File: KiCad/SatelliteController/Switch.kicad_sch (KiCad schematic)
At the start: 22 parts, among them SW1 SW_Push, SW11 SW_Push, SW17 SW_Push, SW18 SW_Push, SW19 SW_Push, SW2 SW_Push, SW20 SW_Push, SW21 SW_Push, SW22 SW_Push, SW23 SW_Push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

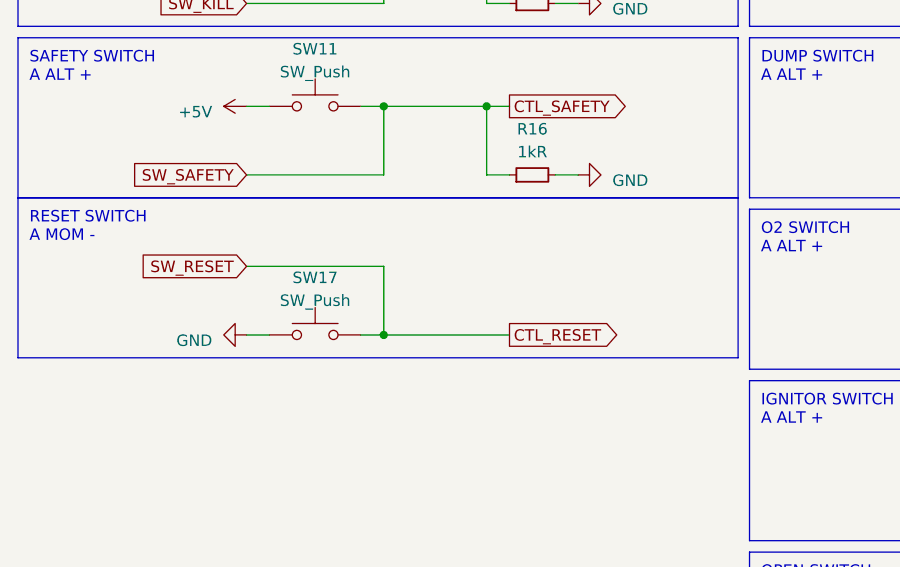
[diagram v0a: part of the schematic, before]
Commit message: サテコンのボード図を作成
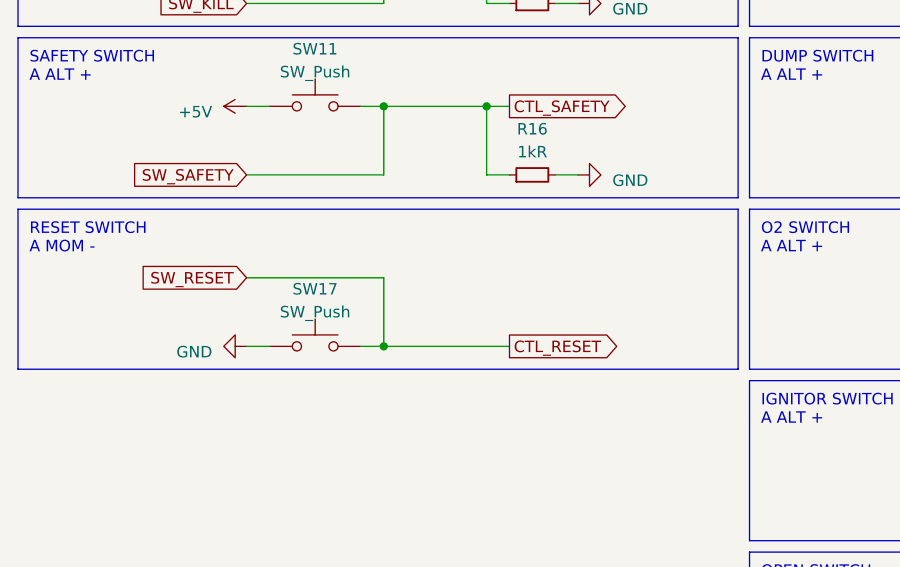
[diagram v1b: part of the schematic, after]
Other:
- moved on the sheet: SW17
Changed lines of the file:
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@@
   (junction (at 53.34 58.42) (diameter 0) (color 0 0 0 0)
   )
-  (junction (at 53.34 83.82) (diameter 0) (color 0 0 0 0)
+  (junction (at 53.34 85.09) (diameter 0) (color 0 0 0 0)
   )
   (junction (at 64.77 39.37) (diameter 0) (color 0 0 0 0)
@@
     (stroke (width 0) (type default))
   )
-  (wire (pts (xy 40.64 83.82) (xy 38.1 83.82))
+  (wire (pts (xy 40.64 85.09) (xy 38.1 85.09))
     (stroke (width 0) (type default))
   )
@@
     (stroke (width 0) (type default))
   )
-  (wire (pts (xy 53.34 76.2) (xy 53.34 83.82))
+  (wire (pts (xy 53.34 77.47) (xy 53.34 85.09))
     (stroke (width 0) (type default))
   )
@@
     (stroke (width 0) (type default))
   )
-  (wire (pts (xy 53.34 83.82) (xy 67.31 83.82))
+  (wire (pts (xy 53.34 85.09) (xy 67.31 85.09))
     (stroke (width 0) (type default))
   )
@@
     (stroke (width 0) (type default))
   )
-  (wire (pts (xy 50.8 83.82) (xy 53.34 83.82))
+  (wire (pts (xy 50.8 85.09) (xy 53.34 85.09))
     (stroke (width 0) (type default))
   )
@@
     (stroke (width 0) (type default))
   )
-  (wire (pts (xy 38.1 76.2) (xy 53.34 76.2))
+  (wire (pts (xy 38.1 77.47) (xy 53.34 77.47))
     (stroke (width 0) (type default))
   )
@@
     (fill (type none))
   )
-  (rectangle (start 12.7 68.58) (end 92.71 86.36)
+  (rectangle (start 12.7 69.85) (end 92.71 87.63)
     (stroke (width 0) (type default))
     (fill (type none))
@@
     (effects (font (size 1.27 1.27)) (justify left bottom))
   )
-  (text "RESET SWITCH\nA MOM -" (at 13.97 73.66 0)
+  (text "RESET SWITCH\nA MOM -" (at 13.97 74.93 0)
     (effects (font (size 1.27 1.27)) (justify left bottom))
   )
@@
     )
   )
-  (global_label "CTL_RESET" (shape output) (at 67.31 83.82 0) (fields_autoplaced)
-    (effects (font (size 1.27 1.27)) (justify left))
-    (property "Intersheetrefs" "${INTERSHEET_REFS}" (at 80.1942 83.82 0)
+  (global_label "CTL_RESET" (shape output) (at 67.31 85.09 0) (fields_autoplaced)
+    (effects (font (size 1.27 1.27)) (justify left))
+    (property "Intersheetrefs" "${INTERSHEET_REFS}" (at 80.1942 85.09 0)
       (effects (font (size 1.27 1.27)) (justify left) hide)
     )
@@
     )
   )
-  (global_label "SW_RESET" (shape input) (at 38.1 76.2 180) (fields_autoplaced)
+  (global_label "SW_RESET" (shape input) (at 38.1 77.47 180) (fields_autoplaced)
     (effects (font (size 1.27 1.27)) (justify right))
-    (property "Intersheetrefs" "${INTERSHEET_REFS}" (at 25.8206 76.2 0)
+    (property "Intersheetrefs" "${INTERSHEET_REFS}" (at 25.8206 77.47 0)
       (effects (font (size 1.27 1.27)) (justify right) hide)
     )
@@
     )
   )
-  (symbol (lib_id "power:GND") (at 38.1 83.82 270) (unit 1)
-    (in_bom yes) (on_board yes) (dnp no) (fields_autoplaced)
-    (property "Reference" "#PWR0104" (at 31.75 83.82 0)
-      (effects (font (size 1.27 1.27)) hide)
-    )
-    (property "Value" "GND" (at 34.29 84.455 90)
+  (symbol (lib_id "power:GND") (at 38.1 85.09 270) (unit 1)
+    (in_bom yes) (on_board yes) (dnp no) (fields_autoplaced)
+    (property "Reference" "#PWR0104" (at 31.75 85.09 0)
+      (effects (font (size 1.27 1.27)) hide)
+    )
+    (property "Value" "GND" (at 34.29 85.725 90)
       (effects (font (size 1.27 1.27)) (justify right))
     )
-    (property "Footprint" "" (at 38.1 83.82 0)
-      (effects (font (size 1.27 1.27)) hide)
-    )
-    (property "Datasheet" "" (at 38.1 83.82 0)
+    (property "Footprint" "" (at 38.1 85.09 0)
+      (effects (font (size 1.27 1.27)) hide)
+    )
+    (property "Datasheet" "" (at 38.1 85.09 0)
       (effects (font (size 1.27 1.27)) hide)
     )
@@
     )
   )
-  (symbol (lib_id "Switch:SW_Push") (at 45.72 83.82 0) (unit 1)
-    (in_bom yes) (on_board yes) (dnp no) (fields_autoplaced)
-    (property "Reference" "SW17" (at 45.72 77.47 0)
-      (effects (font (size 1.27 1.27)))
-    )
-    (property "Value" "SW_Push" (at 45.72 80.01 0)
-      (effects (font (size 1.27 1.27)))
-    )
-    (property "Footprint" "TSRP_Button_Switch_SMD:TVAF06-A020B-R" (at 45.72 78.74 0)
-      (effects (font (size 1.27 1.27)) hide)
-    )
-    (property "Datasheet" "https://akizukidenshi.com/catalog/g/gP-14888/" (at 45.72 78.74 0)
-      (effects (font (size 1.27 1.27)) hide)
-    )
+  (symbol (lib_id "Switch:SW_Push") (at 45.72 85.09 0) (unit 1)
+    (in_bom yes) (on_board yes) (dnp no) (fields_autoplaced)
+    (property "Reference" "SW17" (at 45.72 78.74 0)
+      (effects (font (size 1.27 1.27)))
+    )
+    (property "Value" "SW_Push" (at 45.72 81.28 0)
+      (effects (font (size 1.27 1.27)))
+    )
+    (property "Footprint" "TSRP_Button_Switch_SMD:TVAF06-A020B-R" (at 45.72 80.01 0)
+      (effects (font (size 1.27 1.27)) hide)
+    )
+    (property "Datasheet" "https://akizukidenshi.com/catalog/g/gP-14888/" (at 45.72 80.01 0)
+      (effects (font (size 1.27 1.27)) hide)
+    )

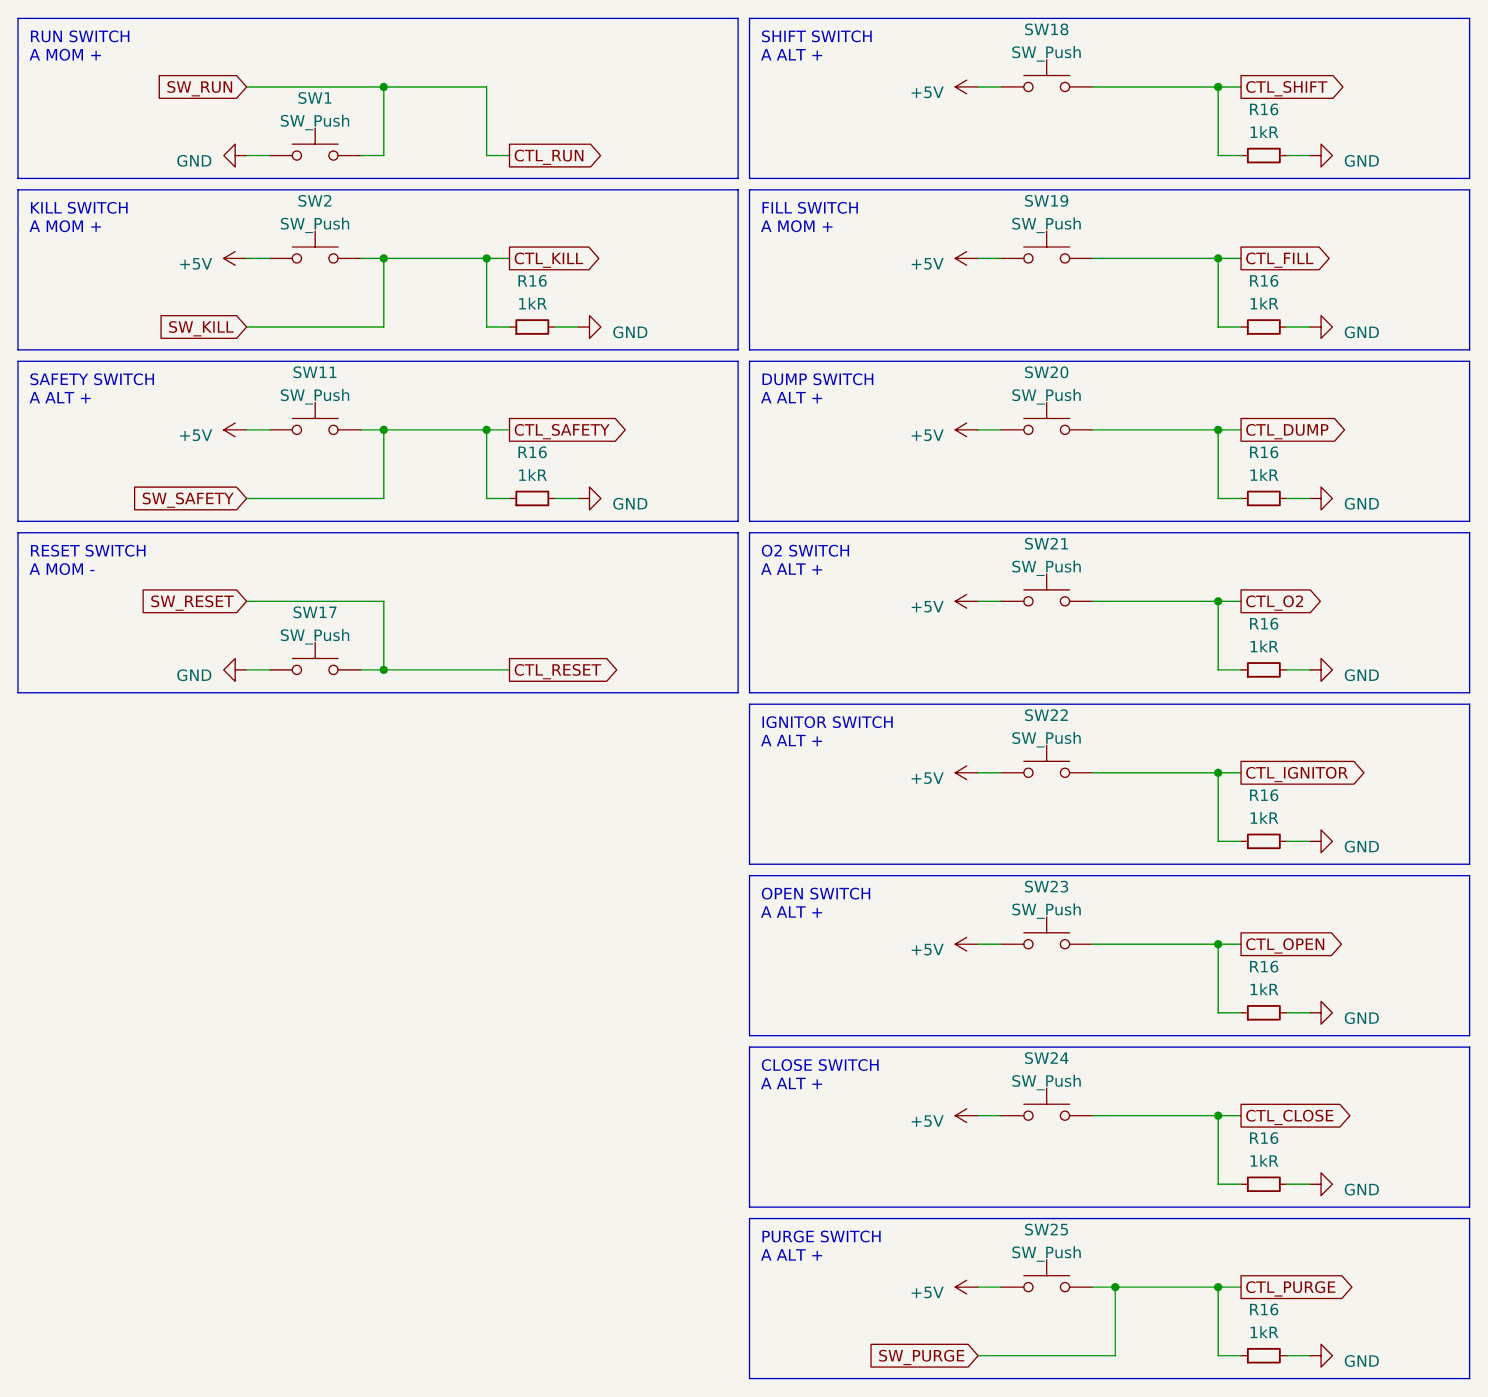
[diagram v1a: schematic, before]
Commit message: サテコンの制御スイッチをプルダウンに変更
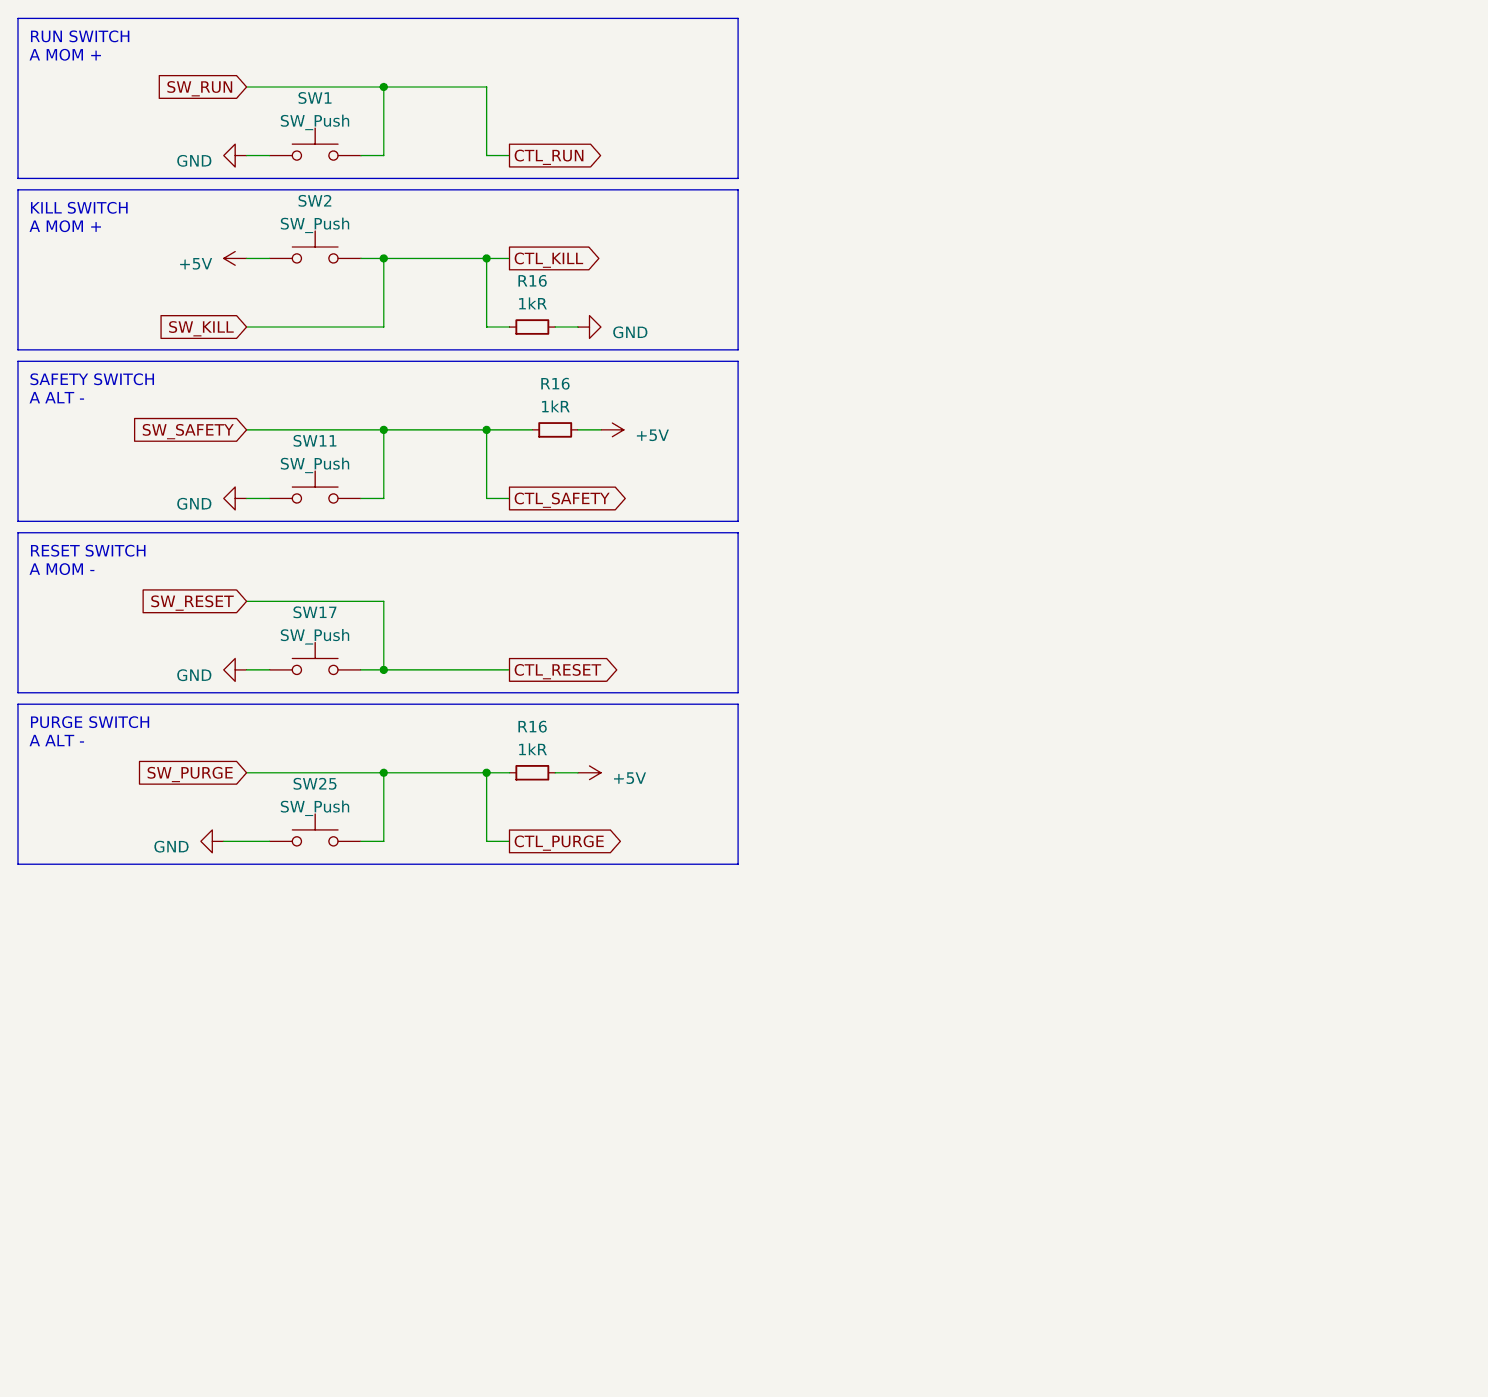
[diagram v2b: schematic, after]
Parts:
- removed R16 (x7): 1kR, Resistor_SMD:R_0603_1608Metric_Pad0.98x0.95mm_HandSolder, symbol Device:R_Small
- removed SW18, SW19, SW20, SW21, SW22, SW23, SW24: SW_Push, Connector_PinHeader_2.54mm:PinHeader_1x02_P2.54mm_Vertical, symbol Switch:SW_Push
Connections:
- net +5V: now also R16.2, R16.2; no longer SW11.1, SW25.1
- net GND: now also SW11.1, SW25.1; no longer R16.2, R16.2
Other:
- note added: "PURGE SWITCH A ALT -"
- note added: "SAFETY SWITCH A ALT -"
- note removed: "CLOSE SWITCH A ALT +"
- note removed: "DUMP SWITCH A ALT +"
- note removed: "FILL SWITCH A MOM +"
- note removed: "IGNITOR SWITCH A ALT +"
- note removed: "O2 SWITCH A ALT +"
- note removed: "OPEN SWITCH A ALT +"
- note removed: "PURGE SWITCH A ALT +"
- note removed: "SAFETY SWITCH A ALT +"
- note removed: "SHIFT SWITCH A ALT +"
- moved on the sheet: R16, SW11, SW25

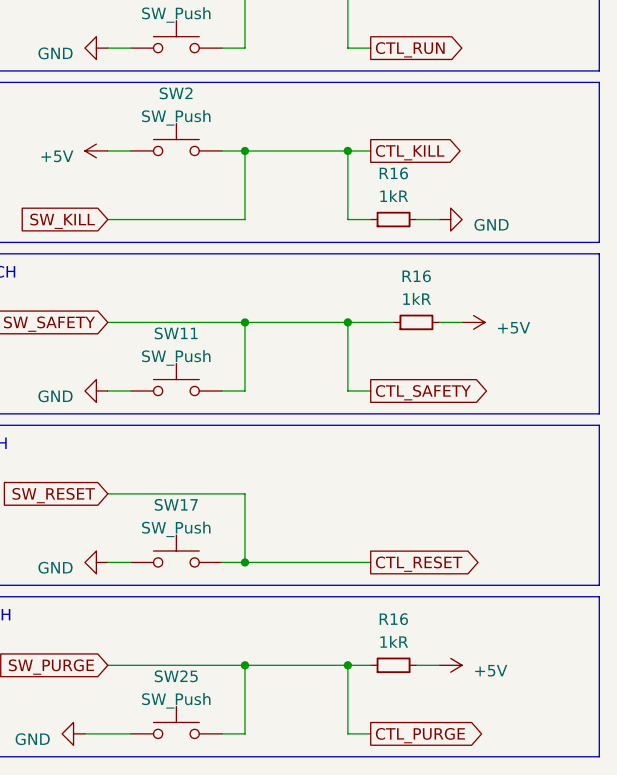
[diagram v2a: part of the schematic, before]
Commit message: サテコンのクリスマスツリーを削除
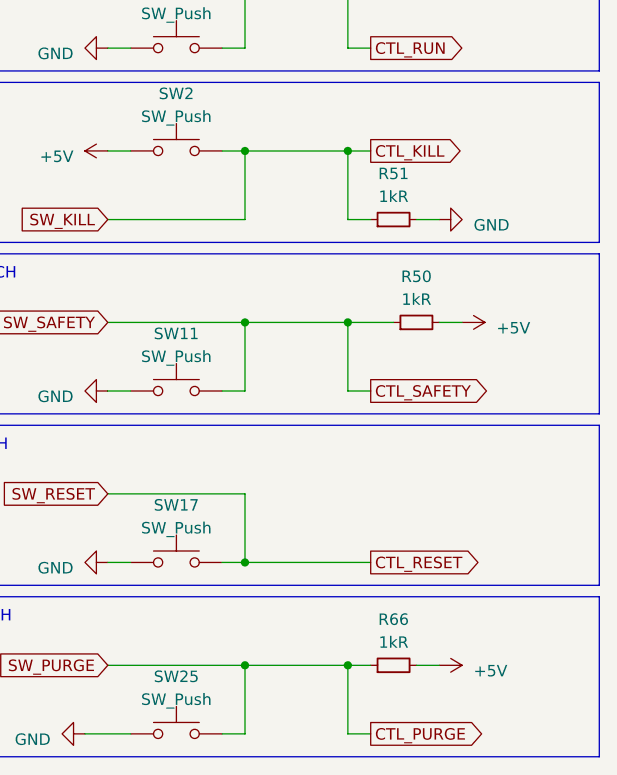
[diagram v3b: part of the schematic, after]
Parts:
- renumbered R16 to R50, R16 to R51, R16 to R66

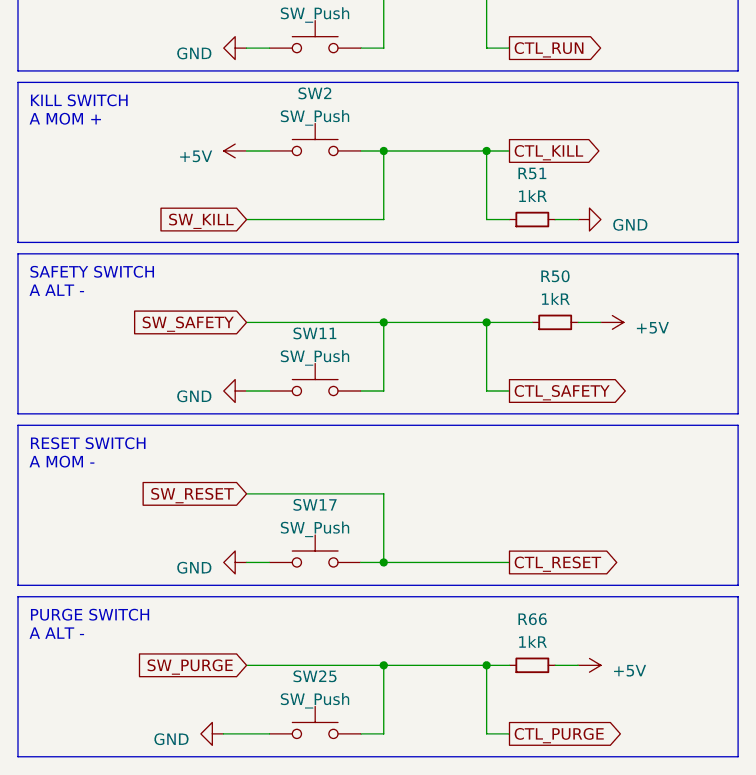
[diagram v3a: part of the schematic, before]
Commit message: 電磁弁制御回路を整理
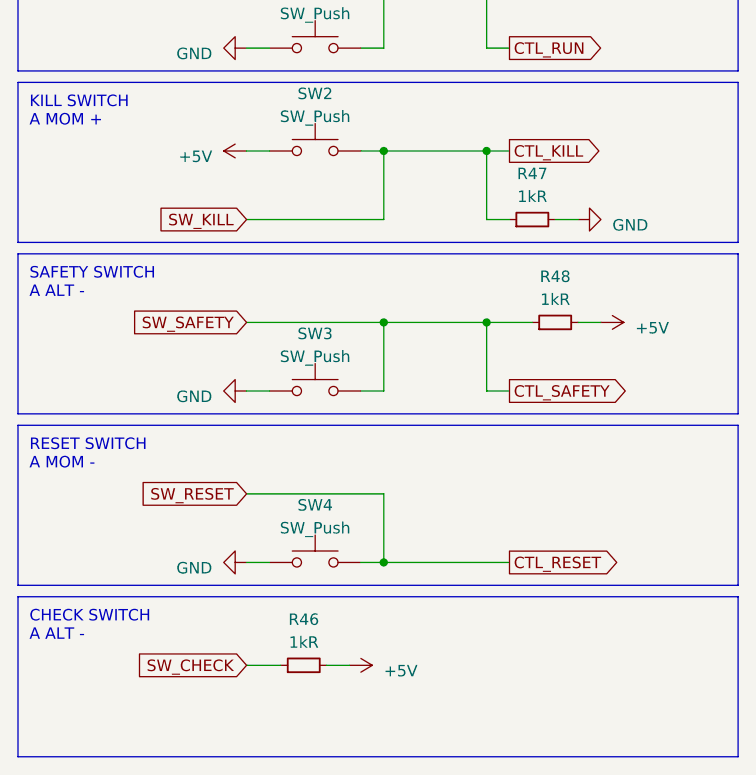
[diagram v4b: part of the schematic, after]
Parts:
- removed SW25: SW_Push, Connector_PinHeader_2.54mm:PinHeader_1x02_P2.54mm_Vertical, symbol Switch:SW_Push
- renumbered R66 to R46, R51 to R47, R50 to R48, SW11 to SW3, SW17 to SW4
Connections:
- net CTL_PURGE renamed SW_CHECK
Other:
- note added: "CHECK SWITCH A ALT -"
- note removed: "PURGE SWITCH A ALT -"
- moved on the sheet: R46
